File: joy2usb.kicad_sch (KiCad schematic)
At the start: 17 parts, among them J1 DB9_Male, J2 Conn_02x04_Odd_Even, SW1 RST, SW2 C64MODESW, U1 Arduino_Pro_Micro

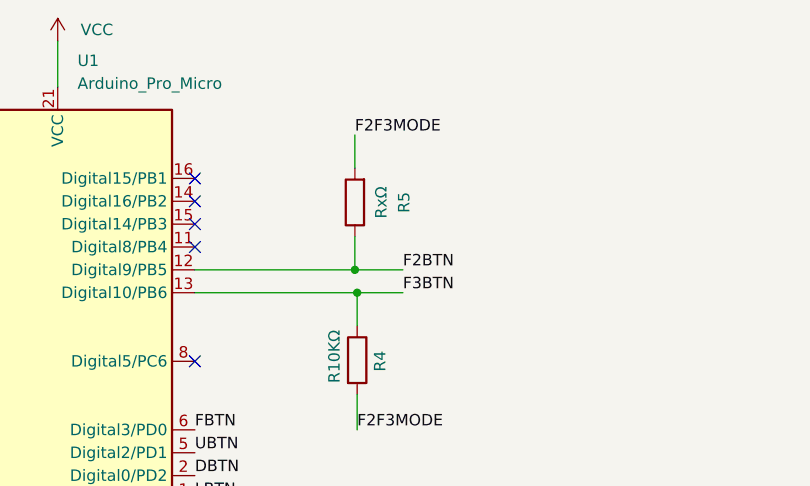
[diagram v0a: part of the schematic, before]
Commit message: added teardrops
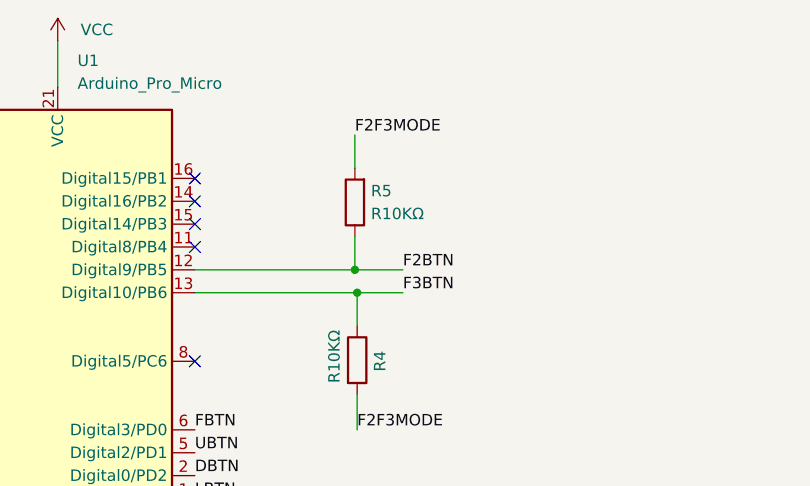
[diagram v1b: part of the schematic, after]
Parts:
- R5: value RxΩ -> R10KΩ
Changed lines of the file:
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@@
   (title_block
     (title "joy2usb")
-    (rev "6.2")
+    (rev "6.3")
     (company "mistepien@wp.pl")
   )
@@
     (pin "1")
     (instances
-      (project "joy2usb-simple"
+      (project "joy2usb"
         (path "/597d0ee1-c37c-44ab-8511-e93942971702"
           (reference "#PWR019") (unit 1)
@@
     )
     (instances
-      (project "joy2usb-simple"
+      (project "joy2usb"
         (path "/597d0ee1-c37c-44ab-8511-e93942971702"
           (reference "H1") (unit 1)
@@
     (pin "2")
     (instances
-      (project "joy2usb-simple"
+      (project "joy2usb"
         (path "/597d0ee1-c37c-44ab-8511-e93942971702"
           (reference "D2") (unit 1)
@@
     (pin "1")
     (instances
-      (project "joy2usb-simple"
+      (project "joy2usb"
         (path "/597d0ee1-c37c-44ab-8511-e93942971702"
           (reference "#PWR025") (unit 1)
@@
     (pin "1")
     (instances
-      (project "joy2usb-simple"
+      (project "joy2usb"
         (path "/597d0ee1-c37c-44ab-8511-e93942971702"
           (reference "#PWR07") (unit 1)
@@
     (pin "1")
     (instances
-      (project "joy2usb-simple"
+      (project "joy2usb"
         (path "/597d0ee1-c37c-44ab-8511-e93942971702"
           (reference "#FLG01") (unit 1)
@@
     (pin "2")
     (instances
-      (project "joy2usb-simple"
+      (project "joy2usb"
         (path "/597d0ee1-c37c-44ab-8511-e93942971702"
           (reference "D3") (unit 1)
@@
     (pin "2")
     (instances
-      (project "joy2usb-simple"
+      (project "joy2usb"
         (path "/597d0ee1-c37c-44ab-8511-e93942971702"
           (reference "R1") (unit 1)
@@
     (pin "1")
     (instances
-      (project "joy2usb-simple"
+      (project "joy2usb"
         (path "/597d0ee1-c37c-44ab-8511-e93942971702"
           (reference "#PWR018") (unit 1)
@@
     (pin "9")
     (instances
-      (project "joy2usb-simple"
+      (project "joy2usb"
         (path "/597d0ee1-c37c-44ab-8511-e93942971702"
           (reference "U1") (unit 1)
@@
     )
     (instances
-      (project "joy2usb-simple"
+      (project "joy2usb"
         (path "/597d0ee1-c37c-44ab-8511-e93942971702"
           (reference "H4") (unit 1)
@@
     (pin "1")
     (instances
-      (project "joy2usb-simple"
+      (project "joy2usb"
         (path "/597d0ee1-c37c-44ab-8511-e93942971702"
           (reference "#FLG02") (unit 1)
@@
     (pin "2")
     (instances
-      (project "joy2usb-simple"
+      (project "joy2usb"
         (path "/597d0ee1-c37c-44ab-8511-e93942971702"
           (reference "D1") (unit 1)
@@
     (pin "1")
     (instances
-      (project "joy2usb-simple"
+      (project "joy2usb"
         (path "/597d0ee1-c37c-44ab-8511-e93942971702"
           (reference "#PWR06") (unit 1)
@@
     (pin "1")
     (instances
-      (project "joy2usb-simple"
+      (project "joy2usb"
         (path "/597d0ee1-c37c-44ab-8511-e93942971702"
           (reference "#PWR017") (unit 1)
@@
     (pin "3")
     (instances
-      (project "joy2usb-simple"
+      (project "joy2usb"
         (path "/597d0ee1-c37c-44ab-8511-e93942971702"
           (reference "SW2") (unit 1)
@@
     (pin "9")
     (instances
-      (project "joy2usb-simple"
+      (project "joy2usb"
         (path "/597d0ee1-c37c-44ab-8511-e93942971702"
           (reference "J1") (unit 1)
@@
   (symbol (lib_id "Device:R") (at 164.592 43.688 180) (unit 1)
     (in_bom yes) (on_board yes) (dnp no) (fields_autoplaced)
-    (property "Reference" "R5" (at 170.053 43.688 90)
-      (effects (font (size 1.27 1.27)))
-    )
-    (property "Value" "RxΩ" (at 167.513 43.688 90)
-      (effects (font (size 1.27 1.27)))
+    (property "Reference" "R5" (at 166.37 42.418 0)
+      (effects (font (size 1.27 1.27)) (justify right))
+    )
+    (property "Value" "R10KΩ" (at 166.37 44.958 0)
+      (effects (font (size 1.27 1.27)) (justify right))
     )
     (property "Footprint" "misc:R_Axial_DIN0207_L6.3mm_D2.5mm_P10.16mm_Horizontal_Oval" (at 166.37 43.688 90)
@@
     (pin "2")
     (instances
-      (project "joy2usb-simple"
+      (project "joy2usb"
         (path "/597d0ee1-c37c-44ab-8511-e93942971702"
           (reference "R5") (unit 1)
@@
     (pin "2")
     (instances
-      (project "joy2usb-simple"
+      (project "joy2usb"
         (path "/597d0ee1-c37c-44ab-8511-e93942971702"
           (reference "R2") (unit 1)
@@
     (pin "1")
     (instances
-      (project "joy2usb-simple"
+      (project "joy2usb"
         (path "/597d0ee1-c37c-44ab-8511-e93942971702"
           (reference "#PWR016") (unit 1)
@@
     (pin "1")
     (instances
-      (project "joy2usb-simple"
+      (project "joy2usb"
         (path "/597d0ee1-c37c-44ab-8511-e93942971702"
           (reference "#PWR03") (unit 1)
@@
     (pin "8")
     (instances
-      (project "joy2usb-simple"
+      (project "joy2usb"
         (path "/597d0ee1-c37c-44ab-8511-e93942971702"
           (reference "J2") (unit 1)
@@
     (pin "2")
     (instances
-      (project "joy2usb-simple"
+      (project "joy2usb"
         (path "/597d0ee1-c37c-44ab-8511-e93942971702"
           (reference "R3") (unit 1)
@@
     (pin "1")
     (instances
-      (project "joy2usb-simple"
+      (project "joy2usb"
         (path "/597d0ee1-c37c-44ab-8511-e93942971702"
           (reference "#PWR02") (unit 1)
@@
     )
     (instances
-      (project "joy2usb-simple"
+      (project "joy2usb"
         (path "/597d0ee1-c37c-44ab-8511-e93942971702"
           (reference "H3") (unit 1)
@@
     (pin "1")
     (instances
-      (project "joy2usb-simple"
+      (project "joy2usb"
         (path "/597d0ee1-c37c-44ab-8511-e93942971702"
           (reference "#PWR020") (unit 1)
@@
     (pin "2")
     (instances
-      (project "joy2usb-simple"
+      (project "joy2usb"
         (path "/597d0ee1-c37c-44ab-8511-e93942971702"
           (reference "R4") (unit 1)
@@
     )
     (instances
-      (project "joy2usb-simple"
+      (project "joy2usb"
         (path "/597d0ee1-c37c-44ab-8511-e93942971702"
           (reference "H2") (unit 1)
@@
     (pin "1")
     (instances
-      (project "joy2usb-simple"
+      (project "joy2usb"
         (path "/597d0ee1-c37c-44ab-8511-e93942971702"
           (reference "#PWR01") (unit 1)
@@
     (pin "1")
     (instances
-      (project "joy2usb-simple"
+      (project "joy2usb"
         (path "/597d0ee1-c37c-44ab-8511-e93942971702"
           (reference "#PWR026") (unit 1)
@@
     (pin "2")
     (instances
-      (project "joy2usb-simple"
+      (project "joy2usb"
         (path "/597d0ee1-c37c-44ab-8511-e93942971702"
           (reference "SW1") (unit 1)
@@
     (pin "1")
     (instances
-      (project "joy2usb-simple"
+      (project "joy2usb"
         (path "/597d0ee1-c37c-44ab-8511-e93942971702"
           (reference "#PWR027") (unit 1)
